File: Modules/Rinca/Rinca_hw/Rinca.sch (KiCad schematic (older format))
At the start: 47 parts

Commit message: Rinca brd added
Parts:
- removed C3: 1u, symbol C
- removed XL3: CONN_2, symbol CONN_2
- removed XL?: CONN_NOKIA_LCD, symbol CONN_NOKIA_LCD
- added C1, C12: 0.1u, symbol C
- added C10: 1000u, symbol CP
- added C14, C2: 10u, symbol C
- added C15: 1000pF, symbol C
- added C16: 1u, symbol C
- added DA1: IPS6041, symbol IPS6041
- added DA3: TPS71533, symbol TPS71533
- added DA4: LP2951, symbol LP2951
- added F1, F2, F3, F4: FUSE0R, symbol FUSE0R
- added R2: 51R, RES_0603, symbol R
- added R3: 200k, symbol R
- added R4: 120k, symbol R
- added SW1: SWITCH, symbol SWITCH
- added SW2, SW3, SW4: BUTTON, symbol BUTTON
- added XL1: CONN_1, symbol CONN_1
- added XL5: BARREL_SOCKET, symbol BARREL_SOCKET
- added XL6: CONN_3, symbol CONN_3
- added XL?: CONN_NOKIA_LCD10, symbol CONN_NOKIA_LCD10
- R1: value 22R -> 10k
- gave numbers to parts that had none: 3
- renumbered C10 to C11, C12 to C13, C4 to C17, C11 to C18, C13 to C19, C19 to C22, C20 to C23, C21 to C24, C22 to C25, C23 to C26, C24 to C27, C25 to C28, C1 to C3, C2 to C4, DA3 to DA2, DD3 to DD2, DD2 to DD3, R8 to R5, R2 to R6, R3 to R8, R4 to R9, TP2 to TP1, XL1 to XL2, XL2 to XL3
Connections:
- net labels added: BUTTON1, BUTTON2, BUTTON3, Ch1_ERROR, Ch1_IN, Ch1_OUT, GPIO0, RX1
- net labels removed: Sound
- wire segments 160 -> 216
- no-connect marks 18 -> 19
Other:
- note added: "3.3V power regulator\n(Choose one or another)"
- moved on the sheet: B1, C17, C18, C19, DD2, R8, R9, XL2, XL3

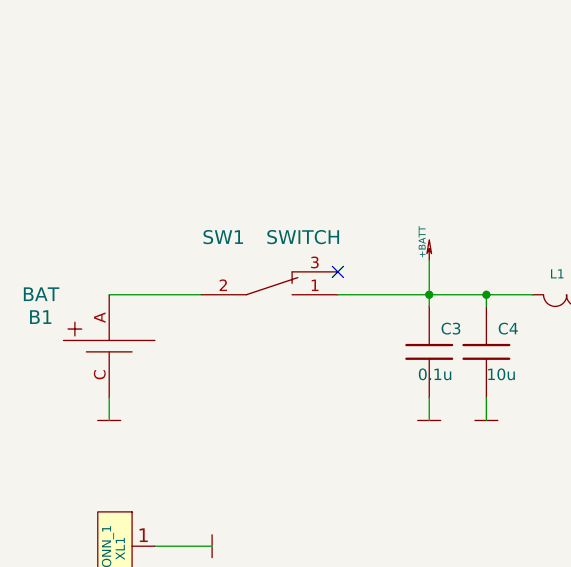
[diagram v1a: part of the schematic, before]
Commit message: 
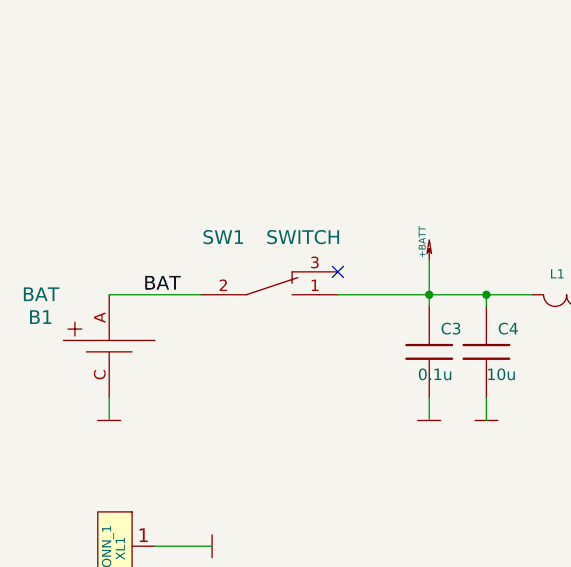
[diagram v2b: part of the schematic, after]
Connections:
- net labels added: BAT
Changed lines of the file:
@@
-EESchema Schematic File Version 2  date 10/04/2013 14:54:21
+EESchema Schematic File Version 2  date 10/04/2013 23:36:24
 LIBS:Connectors_kl
 LIBS:pcb_details
@@
 	1    0    0    -1
 $EndComp
+Text Label 1950 9200 0    60   ~ 0
+BAT
 $EndSCHEMATC
